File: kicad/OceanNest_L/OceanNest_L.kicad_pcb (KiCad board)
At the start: 2 copper layers, 103.5 x 88.7 mm, 35 parts, among them J1 TRRS_MJ-4PP-9, SW1 SW_Push, SW10 SW_Push, SW11 SW_Push, SW12 SW_Push, SW13 SW_Push, SW14 RotaryEncoder, SW2 SW_Push, SW3 SW_Push, SW4 SW_Push, SW5 SW_Push, SW6 SW_Push, SW7 SW_Push, SW8 SW_Push, SW9 SW_Push, U1 XIAO-RP2040-DIP

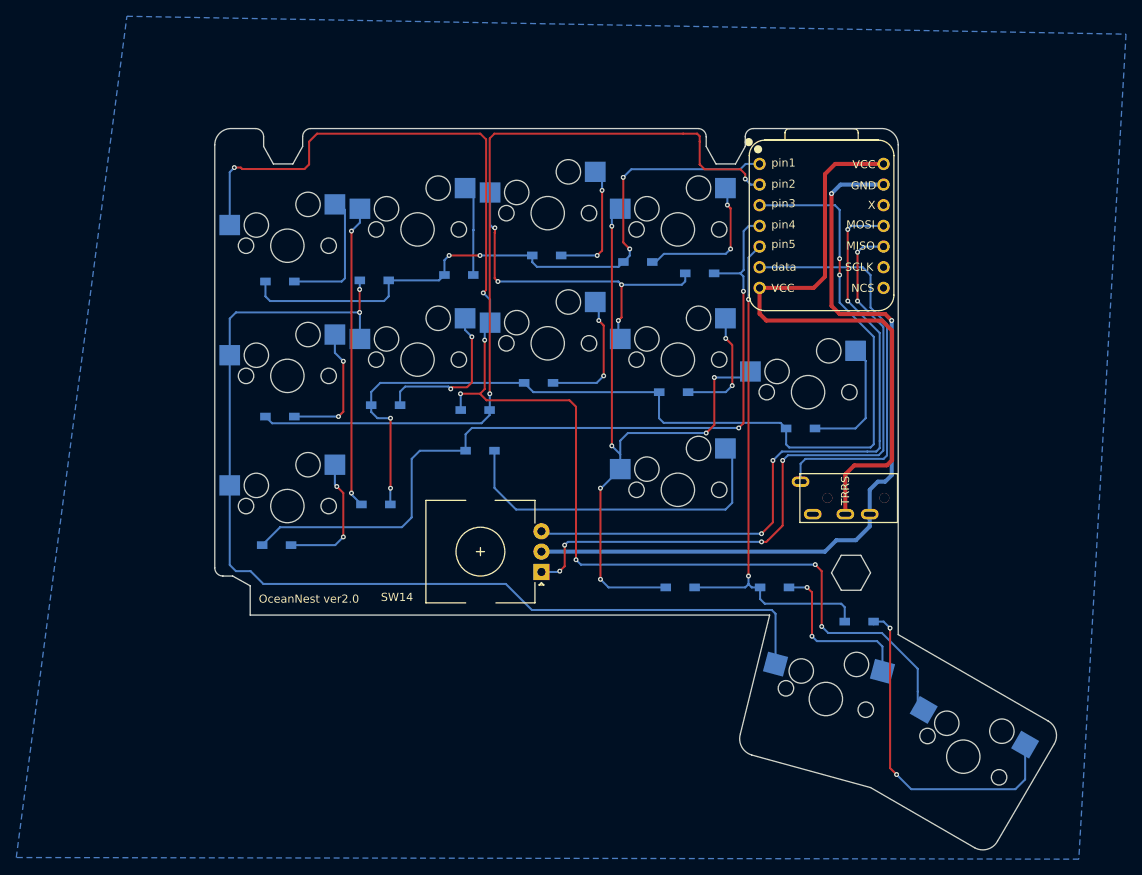
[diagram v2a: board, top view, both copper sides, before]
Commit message: feat: add new OceanNest_L and OceanNest_R PCB and project files for enhanced design capabilities
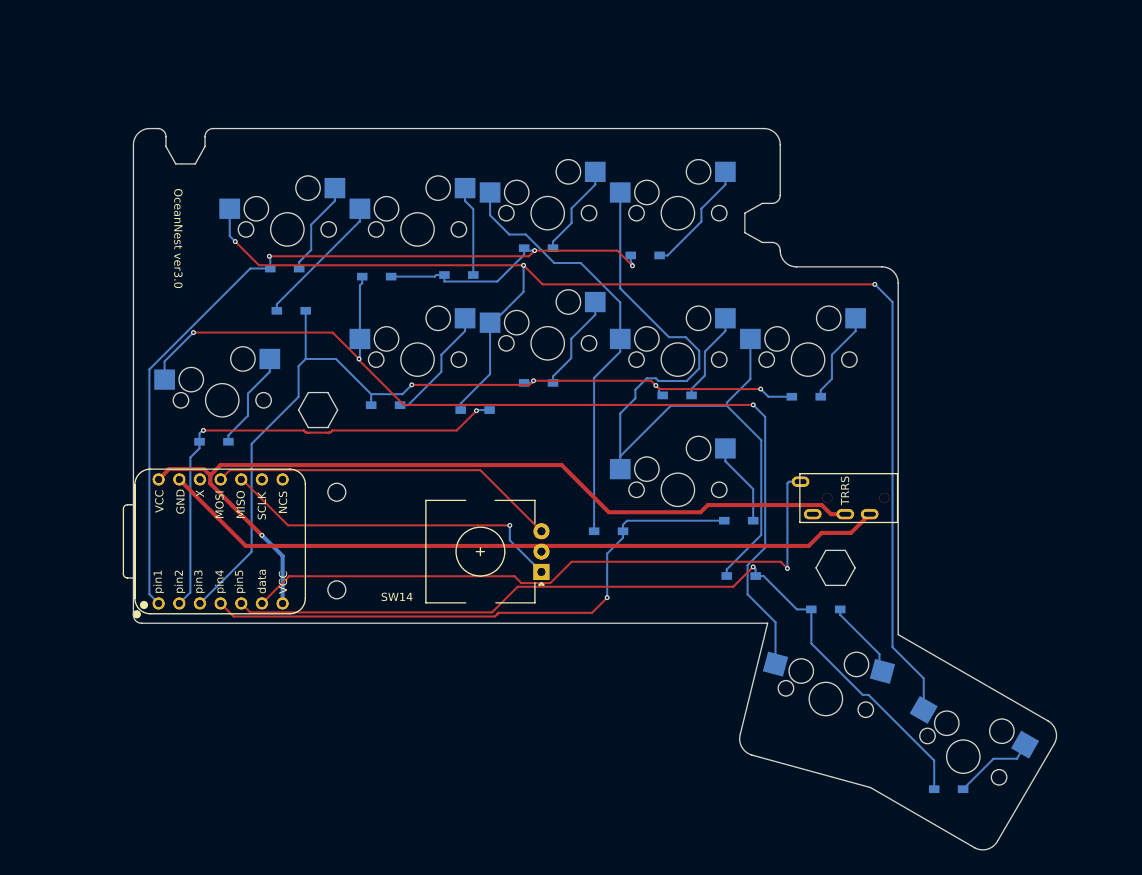
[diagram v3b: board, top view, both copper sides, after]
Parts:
- removed D13: D, kbd_Parts:Diode_SMD
- removed SW10: SW_Push, takashicompany:CherryMX_Hotswap_16m
- added hole2: Val**, kbd_Hole:m2_Spacer_Hole_hex, F.Cu at (72.7, 134.6)
- added hole3: Val**, kbd_Hole:m2_Screw_Hole, F.Cu at (75.0, 144.7)
- added hole4: Val**, kbd_Hole:m2_Screw_Hole, F.Cu at (75.0, 156.7)
- moved U1 83.4 mm to (60.7, 150.7), turned to 90 degrees
- moved D14 33.6 mm to (108.4, 149.5)
- moved D15 32.9 mm to (124.4, 148.2)
- moved D10 26.0 mm to (69.4, 122.4)
- moved D17 23.4 mm to (150.2, 181.2)
- moved D6 8.67 mm to (59.9, 138.5)
- moved SW5 8.54 mm to (60.9, 133.4)
- moved D18 7.63 mm to (124.7, 155.0)
- moved D16 6.85 mm to (135.1, 159.1)
- moved SW9 4.00 mm to (132.9, 128.4)
- moved D12 3.96 mm to (132.7, 133.0)
- moved SW1 2.00 mm to (68.9, 112.4)
- moved SW4 2.00 mm to (116.9, 110.4)
- moved hole1 1.99 mm to (136.3, 154.0)
- moved D2 1.71 mm to (68.6, 117.2)
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- renumbered Ref** to hole1
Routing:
- net pin2: track 100.7 -> 59.1 mm
- net REa: track 83.6 -> 42.7 mm, vias 6 -> 1
- net REb: track 83.6 -> 43.0 mm, vias 4 -> 0
- net pin5: track 64.5 -> 104.3 mm, vias 2 -> 1
- net pin1: track 80.4 -> 118.6 mm, vias 4 -> 3
- net Net-(D17-A): track 42.4 -> 10.2 mm, vias 2 -> 0
- net Net-(D15-A): track 42.3 -> 10.3 mm
- net VCC: track 76.5 -> 108.4 mm, vias 0 -> 1
- net data: track 50.3 -> 79.9 mm, vias 0 -> 1
- net pin4: track 100.1 -> 71.8 mm, vias 2 -> 1
- net Net-(D10-K): track 37.3 -> 16.8 mm, vias 2 -> 0
- net pin3: track 125.1 -> 108.6 mm
- net Net-(D13-A): track 16.1 -> 0.00 mm, vias 2 -> 0
- net Net-(D18-K): track 80.5 -> 96.1 mm, vias 6 -> 0
- net Net-(D16-A): track 20.7 -> 9.77 mm, vias 2 -> 0
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- removed copper zone on B.Cu, net GND
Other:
- board size 103.5 x 88.7 mm -> 113.5 x 88.7 mm
- board text added: "OceanNest ver3.0"
- board text removed: "OceanNest ver2.0"
